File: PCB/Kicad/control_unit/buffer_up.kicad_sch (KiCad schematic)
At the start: 2 parts, among them U16 74HC245, U17 74HC245

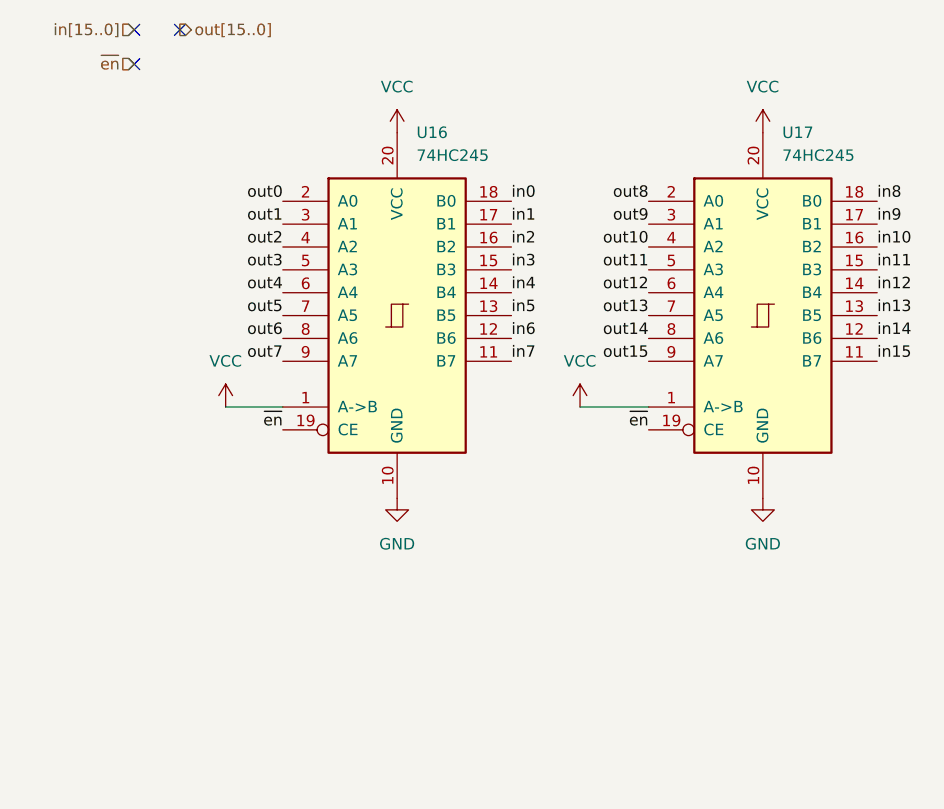
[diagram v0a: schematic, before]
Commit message: control unit schematic
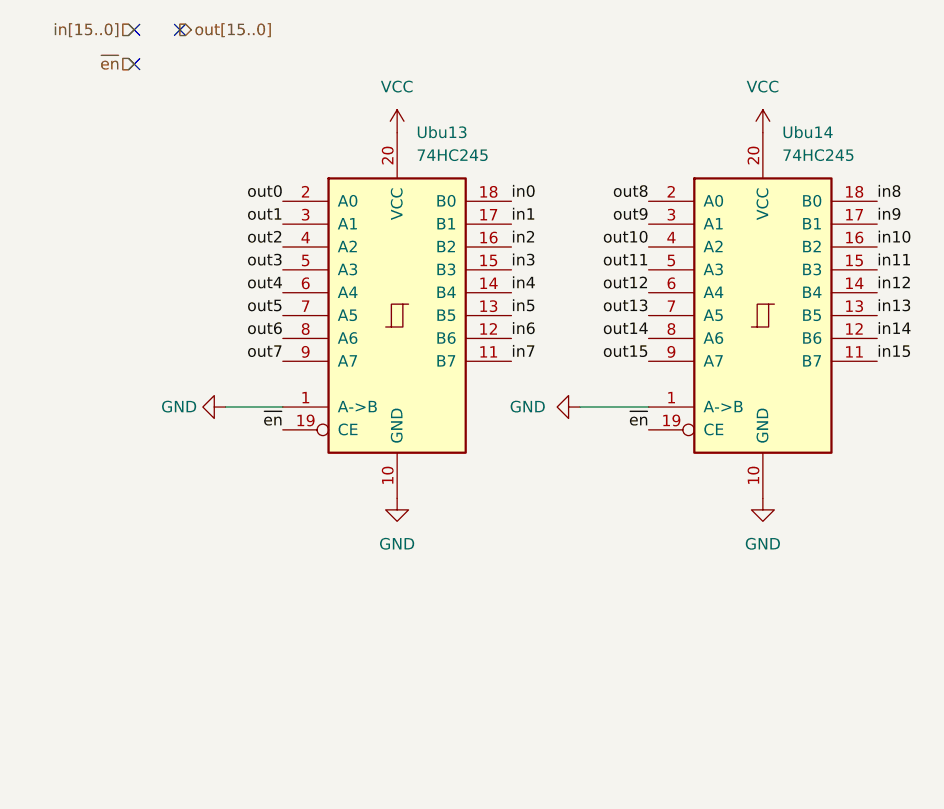
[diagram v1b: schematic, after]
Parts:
- Ubu13: renamed from U16; footprint (none) -> Package_SO:SOIC-20W_7.5x12.8mm_P1.27mm
- Ubu14: renamed from U17; footprint (none) -> Package_SO:SOIC-20W_7.5x12.8mm_P1.27mm
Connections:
- net GND: now also Ubu13.1 (A->B), Ubu14.1 (A->B)
- net VCC: no longer Ubu13.1 (A->B), Ubu14.1 (A->B)
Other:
- company: (none) -> AGH Logic Unit
- title: (none) -> Buffer Down -> Top

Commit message: control unit update
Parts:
- added Cbd12, Cbd13: 100nF, Capacitor_SMD:C_0402_1005Metric, symbol Device:C
- Ubu13, Ubu14: value 74HC245 -> 74245; footprint Package_SO:SOIC-20W_7.5x12.8mm_P1.27mm -> Package_SO:TSSOP-20_4.4x6.5mm_P0.65mm
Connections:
- net GND: now also Cbd12.2, Cbd13.2
- net VCC: now also Cbd12.1, Cbd13.1
